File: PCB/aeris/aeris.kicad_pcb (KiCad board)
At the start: 2 copper layers, 112 x 82 mm, 47 parts, among them J1 PMSA003A, J2 SHT45, J3 LPS22HB, J4 SCD40, J5 SGP41, J6 USB-C Input, J7 OUT, Q1 BSS138, Q2 BSS138, U1 ESP32-C6-SUPERMINI, U2 74AHCT244

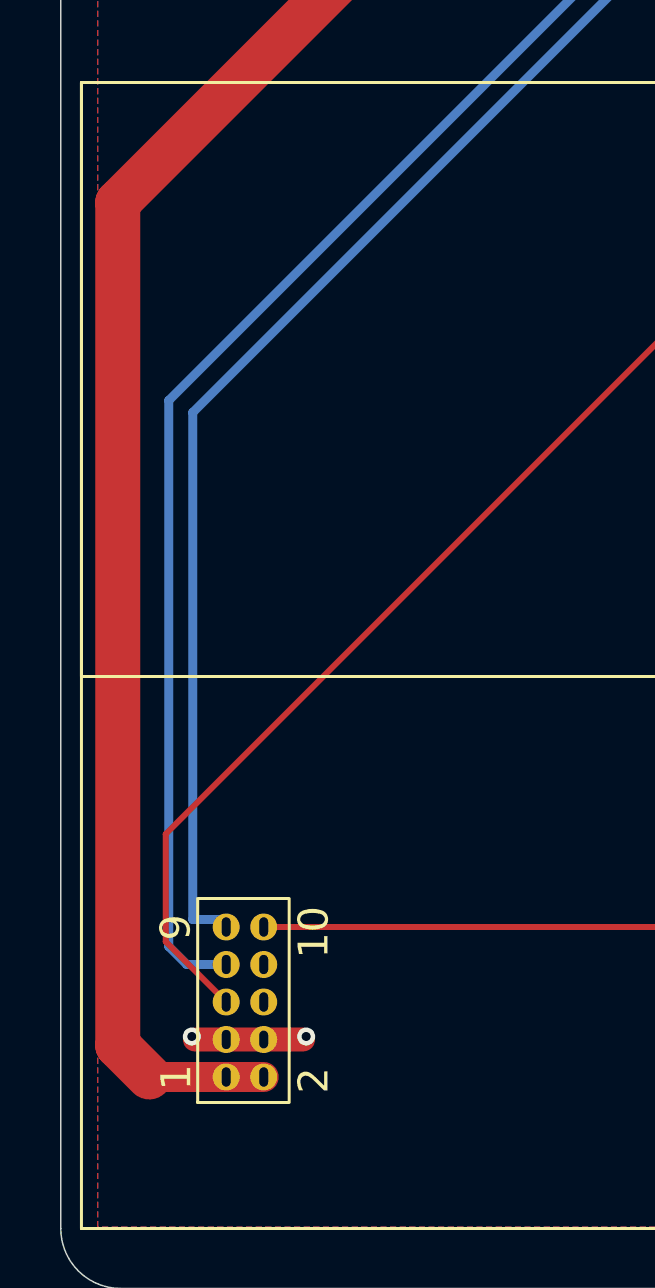
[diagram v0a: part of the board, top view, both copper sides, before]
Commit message: feat: Implement WiFi WebSocket logging for real-time console output
- Added WiFi logging functionality to broadcast logs over WebSocket.
- Introduced configuration options in board.h for enabling/disabling logging and setting WiFi credentials.
- Created wifi_log.c and wifi_log.h for handling WiFi connections and WebSocket communication.
- Updated led_indicator.c to use a shared RMT channel for LED control.
- Modified esp_zb_aeris.c to initialize WiFi logging during app startup.
- Adjusted aeris_driver.h for I2C address corrections and driver inclusions.
- Enhanced board.h with debug flags and WiFi logging configuration.
- Cleaned up unnecessary code in esp_zb_aeris.c related to LED attributes.
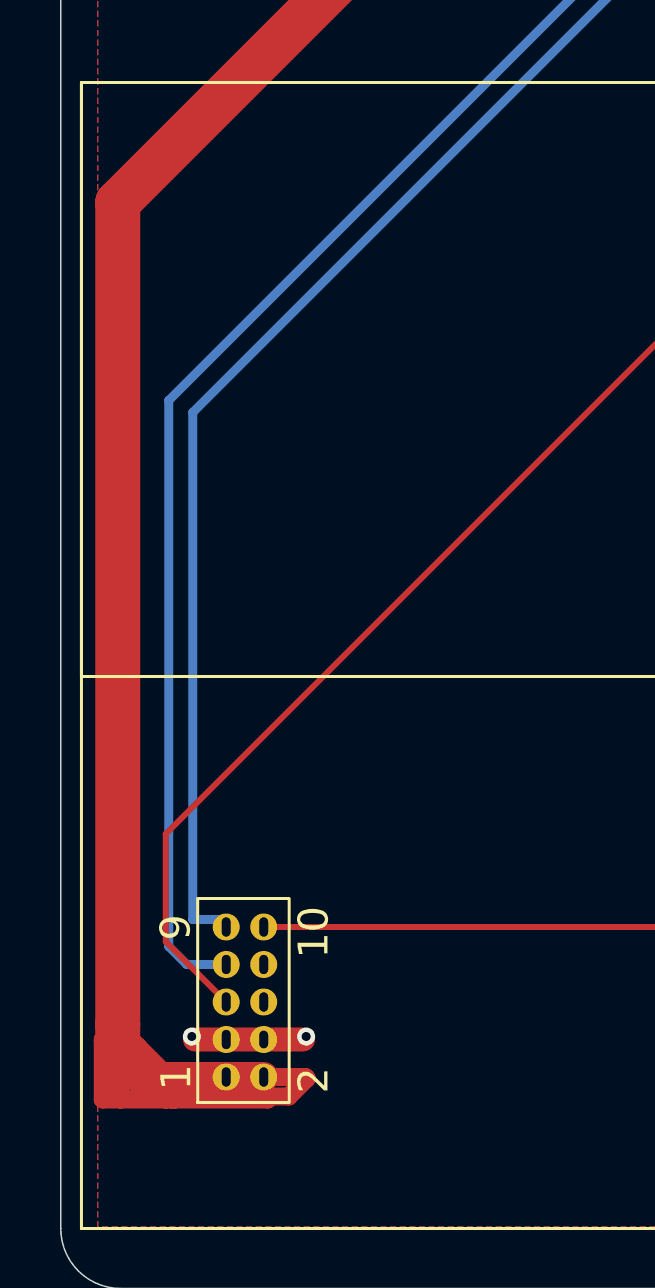
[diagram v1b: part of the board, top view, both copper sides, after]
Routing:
- net +5V: track 247.5 -> 264.0 mm
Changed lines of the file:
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@@
+	)
+	(segment
+		(start 37.95 102.95)
+		(end 37.25 102.25)
+		(width 1.5)
+		(layer "F.Cu")
+		(net 1)
 	)
 	(segment
@@
 	)
 	(segment
+		(start 43.15 102.95)
+		(end 41.765 102.95)
+		(width 0.6)
+		(layer "F.Cu")
+		(net 1)
+	)
+	(segment
 		(start 67.4 32.2)
 		(end 74.9 32.2)
@@
 	)
 	(segment
+		(start 43.2 103)
+		(end 43.15 102.95)
+		(width 0.6)
+		(layer "F.Cu")
+		(net 1)
+	)
+	(segment
+		(start 38.8 103.7)
+		(end 41.9 103.7)
+		(width 0.6)
+		(layer "F.Cu")
+		(net 1)
+	)
+	(segment
 		(start 138.5 62)
 		(end 138.5 60.75)
@@
 	)
 	(segment
+		(start 42.6 103.6)
+		(end 43.2 103)
+		(width 0.6)
+		(layer "F.Cu")
+		(net 1)
+	)
+	(segment
 		(start 50.775 53.6)
 		(end 50.775 51.625)
@@
 	)
 	(segment
+		(start 38.5 103.7)
+		(end 38.8 103.7)
+		(width 0.6)
+		(layer "F.Cu")
+		(net 1)
+	)
+	(segment
+		(start 37 103.7)
+		(end 36.4 103.7)
+		(width 0.6)
+		(layer "F.Cu")
+		(net 1)
+	)
+	(segment
+		(start 38.8 103.7)
+		(end 38.7 103.7)
+		(width 0.6)
+		(layer "F.Cu")
+		(net 1)
+	)
+	(segment
 		(start 115.7 41.2)
 		(end 118.704 44.204)
@@
 		(end 98.025 36)
 		(width 1.5)
+		(layer "F.Cu")
+		(net 1)
+	)
+	(segment
+		(start 36.4 103.7)
+		(end 36.4 101.7)
+		(width 0.6)
 		(layer "F.Cu")
 		(net 1)
@@
 	)
 	(segment
+		(start 37.95 103.15)
+		(end 38.5 103.7)
+		(width 0.6)
+		(layer "F.Cu")
+		(net 1)
+	)
+	(segment
 		(start 102.3 41.2)
 		(end 115.7 41.2)
@@
 	)
 	(segment
+		(start 36.9 101.9)
+		(end 36.9 101.2)
+		(width 1.5)
+		(layer "F.Cu")
+		(net 1)
+	)
+	(segment
 		(start 50.775 59.925)
 		(end 50.775 53.6)
@@
 		(end 59.5 32.2)
 		(width 1.5)
+		(layer "F.Cu")
+		(net 1)
+	)
+	(segment
+		(start 37.95 102.95)
+		(end 37.95 103.15)
+		(width 0.6)
 		(layer "F.Cu")
 		(net 1)
@@
 	)
 	(segment
-		(start 37.95 102.95)
+		(start 37 102.5)
+		(end 37.25 102.25)
+		(width 0.6)
+		(layer "F.Cu")
+		(net 1)
+	)
+	(segment
+		(start 37.25 102.25)
 		(end 36.9 101.9)
 		(width 1.5)
+		(layer "F.Cu")
+		(net 1)
+	)
+	(segment
+		(start 42 103.6)
+		(end 42.6 103.6)
+		(width 0.6)
+		(layer "F.Cu")
+		(net 1)
+	)
+	(segment
+		(start 36.4 101.7)
+		(end 36.9 101.2)
+		(width 0.6)
 		(layer "F.Cu")
 		(net 1)
@@
 	)
 	(segment
-		(start 36.9 101.9)
+		(start 41.9 103.7)
+		(end 42 103.6)
+		(width 0.6)
+		(layer "F.Cu")
+		(net 1)
+	)
+	(segment
+		(start 38.7 103.7)
+		(end 36.9 101.9)
+		(width 0.6)
+		(layer "F.Cu")
+		(net 1)
+	)
+	(segment
+		(start 37 103.7)
+		(end 37 102.5)
+		(width 0.6)
+		(layer "F.Cu")
+		(net 1)
+	)
+	(segment
+		(start 38.5 103.7)
+		(end 37 103.7)
+		(width 0.6)
+		(layer "F.Cu")
+		(net 1)
+	)
+	(segment
+		(start 36.9 101.2)
 		(end 36.9 73.8)
 		(width 1.5)
@@
 	)
 	(zone
-		(net 19)
-		(net_name "GPIO2")
+		(net 16)
+		(net_name "GPIO19")
 		(layer "F.Cu")
 		(name "$teardrop_padvia$")
 		(hatch none 0.1)
 		(priority 30001)
+		(attr
+			(teardrop
+				(type padvia)
+			)
+		)
+		(connect_pads yes
+			(clearance 0)
+		)
+		(min_thickness 0.0254)
+		(filled_areas_thickness no)
+		(fill yes
+			(thermal_gap 0.5)
+			(thermal_bridge_width 0.5)
+			(island_removal_mode 1)
+			(island_area_min 10)
+		)
+		(polygon
+			(pts
+				(xy 42.656353 98.05) (xy 42.656353 97.85) (xy 42.015007 97.575839) (xy 41.764 97.95) (xy 42.015007 98.324161)
+			)
+		)
+	)
+	(zone
+		(net 1)
+		(net_name "+5V")
+		(layer "F.Cu")
+		(name "$teardrop_padvia$")
+		(hatch none 0.1)
+		(priority 30000)
+		(attr
+			(teardrop
+				(type padvia)
+			)
+		)
+		(connect_pads yes
+			(clearance 0)
+		)
+		(min_thickness 0.0254)
+		(filled_areas_thickness no)
+		(fill yes
+			(thermal_gap 0.5)
+			(thermal_bridge_width 0.5)
+			(island_removal_mode 1)
+			(island_area_min 10)
+		)
+		(polygon
+			(pts
+				(xy 42.656353 103.25) (xy 42.656353 102.65) (xy 41.852791 102.508647) (xy 41.764 102.95) (xy 41.852791 103.391353)
+			)
+		)
+	)
+	(zone
+		(net 19)
+		(net_name "GPIO2")
+		(layer "F.Cu")
+		(name "$teardrop_padvia$")
+		(hatch none 0.1)
+		(priority 30002)
 		(attr
 			(teardrop
@@
 			)
 		)
-	)
-	(zone
-		(net 16)
-		(net_name "GPIO19")
-		(layer "F.Cu")
-		(name "$teardrop_padvia$")
-		(hatch none 0.1)
-		(priority 30000)
-		(attr
-			(teardrop
-				(type padvia)
-			)
-		)
-		(connect_pads yes
-			(clearance 0)
-		)
-		(min_thickness 0.0254)
-		(filled_areas_thickness no)
-		(fill yes
-			(thermal_gap 0.5)
-			(thermal_bridge_width 0.5)
-			(island_removal_mode 1)
-			(island_area_min 10)
-		)
-		(polygon
-			(pts
-				(xy 42.656353 98.05) (xy 42.656353 97.85) (xy 42.015007 97.575839) (xy 41.764 97.95) (xy 42.015007 98.324161)
-			)
-		)

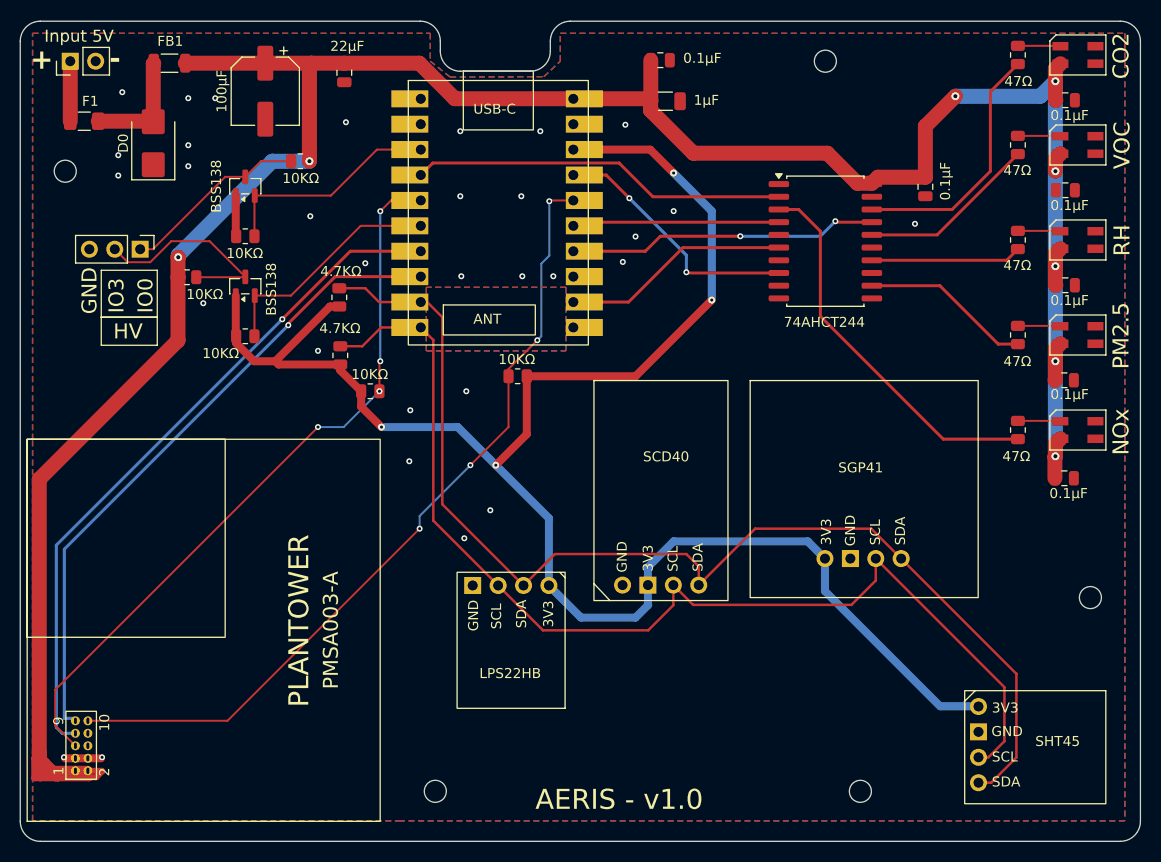
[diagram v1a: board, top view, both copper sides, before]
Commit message: Refactor PCB design and update sensor configurations
- Changed footprint references for LED components to use the correct library.
- Enhanced README with detailed sensor conversion formulas and calibration notes.
- Updated aeris_driver.c to enforce minimum sampling intervals for SGP41 and SCD40 sensors.
- Disabled automatic self-calibration for SCD40 to maintain stable CO2 baseline.
- Adjusted LPS22HB sensor configuration to use one-shot mode for power savings.
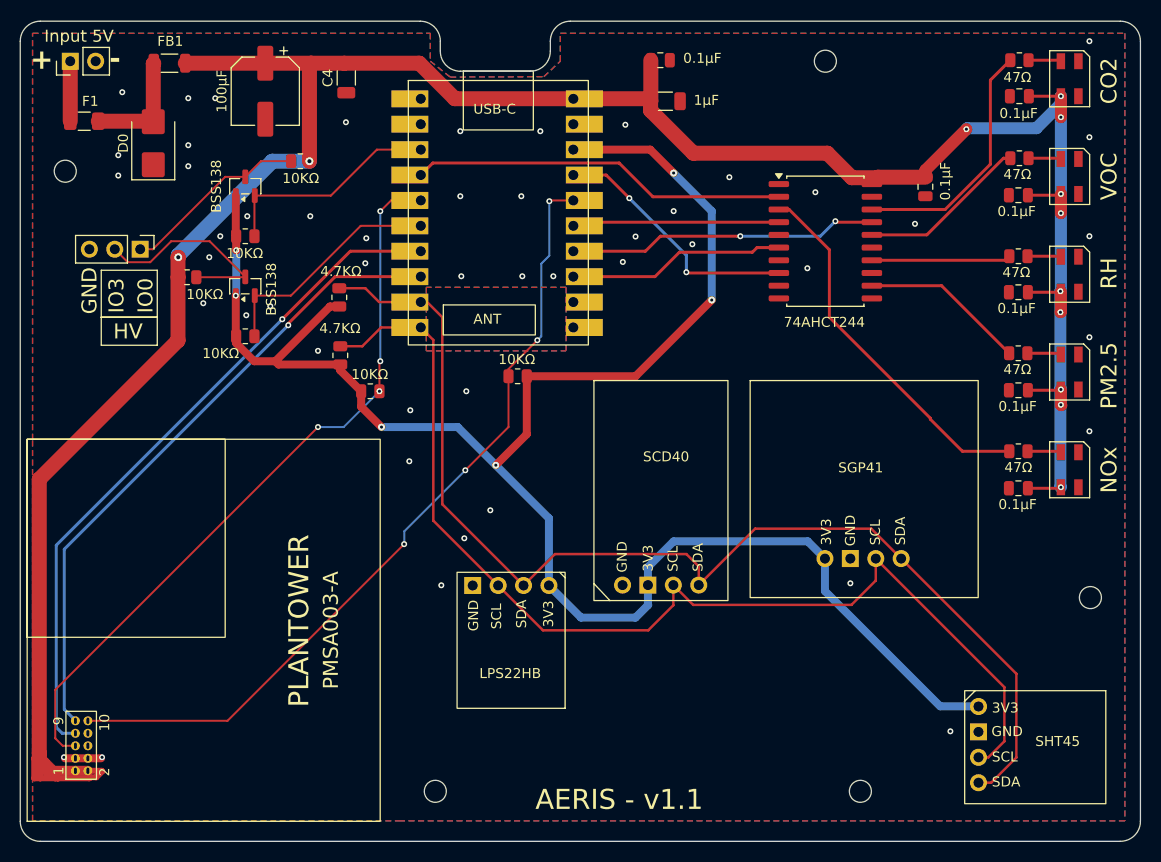
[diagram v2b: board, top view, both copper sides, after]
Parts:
- C4: footprint Capacitor_SMD:C_0805_2012Metric -> Capacitor_SMD:C_1206_3216Metric
- D1, D2, D3, D4, D5: footprint LED_SMD:LED_SK6812MINI_PLCC4_3.5x3.5mm_P1.75mm -> esp32-h2-supermini:LED_SK6812MINI_PLCC4_3.5x3.5mm_P1.75mm
- R3, R4: value 10KΩ -> 10K
- moved C5 4.75 mm to (134.8, 55.1), turned to 180 degrees
- moved C9 4.73 mm to (134.8, 45.4), turned to 180 degrees
- moved C6 4.71 mm to (134.8, 64.9), turned to 180 degrees
- moved C7 4.71 mm to (134.8, 74.7), turned to 180 degrees
- moved C8 4.62 mm to (134.9, 35.5), turned to 180 degrees
- moved D5 4.06 mm to (139.9, 72.8), turned to 90 degrees
- moved D4 3.79 mm to (139.9, 63.1), turned to 90 degrees
- moved D3 3.52 mm to (139.9, 53.3), turned to 90 degrees
- moved D2 3.26 mm to (139.9, 43.5), turned to 90 degrees
- moved D1 2.51 mm to (139.9, 33.8), turned to 90 degrees
- moved R13 2.13 mm to (134.8, 71.0), turned to 0 degrees
- moved R12 1.83 mm to (134.8, 61.2), turned to 0 degrees
- moved R11 1.63 mm to (134.8, 51.5), turned to 0 degrees
- moved R10 1.33 mm to (134.9, 41.7), turned to 0 degrees
- moved C4 0.56 mm to (67.6, 33.7)
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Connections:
- U1 pad 2: GPIO9 -> unconnected-(U1-IO9-Pad2)
- U1 pad 3: unconnected-(U1-IO14-Pad3) -> GPIO14
- U2 pad 6: GPIO9 -> GPIO14
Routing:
- net GPIO9: track 22.8 -> 0.00 mm
- net GPIO14: track 0.00 -> 21.8 mm
- net +3V3: track 179.6 -> 185.5 mm, vias 4 -> 6
- net +5V: track 264.0 -> 269.8 mm, vias 8 -> 12
- net NOx: track 38.4 -> 37.1 mm
- net RH: track 15.1 -> 13.9 mm
- net Net-(D2-DIN): track 4.27 -> 3.27 mm
- net Net-(D1-DIN): track 4.27 -> 3.28 mm
- net VOC: track 17.9 -> 17.0 mm
- net Net-(D3-DIN): track 4.27 -> 3.36 mm
- net Net-(D5-DIN): track 4.27 -> 3.38 mm
- net Net-(D4-DIN): track 4.27 -> 3.40 mm
- net GPIO2: track 73.7 -> 74.5 mm
- net RX: track 65.2 -> 64.7 mm
- net GND: vias 31 -> 49
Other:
- board text added: "AERIS - v1.1"
- board text removed: "AERIS - v1.0"
